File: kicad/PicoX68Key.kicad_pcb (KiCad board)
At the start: 2 copper layers, 33.9 x 69 mm, 21 parts, among them J1 LED_BOARD, J2 MD-70S, Q1 2N7000, Q2 2N7000, Q3 2N7000, U1 Pico

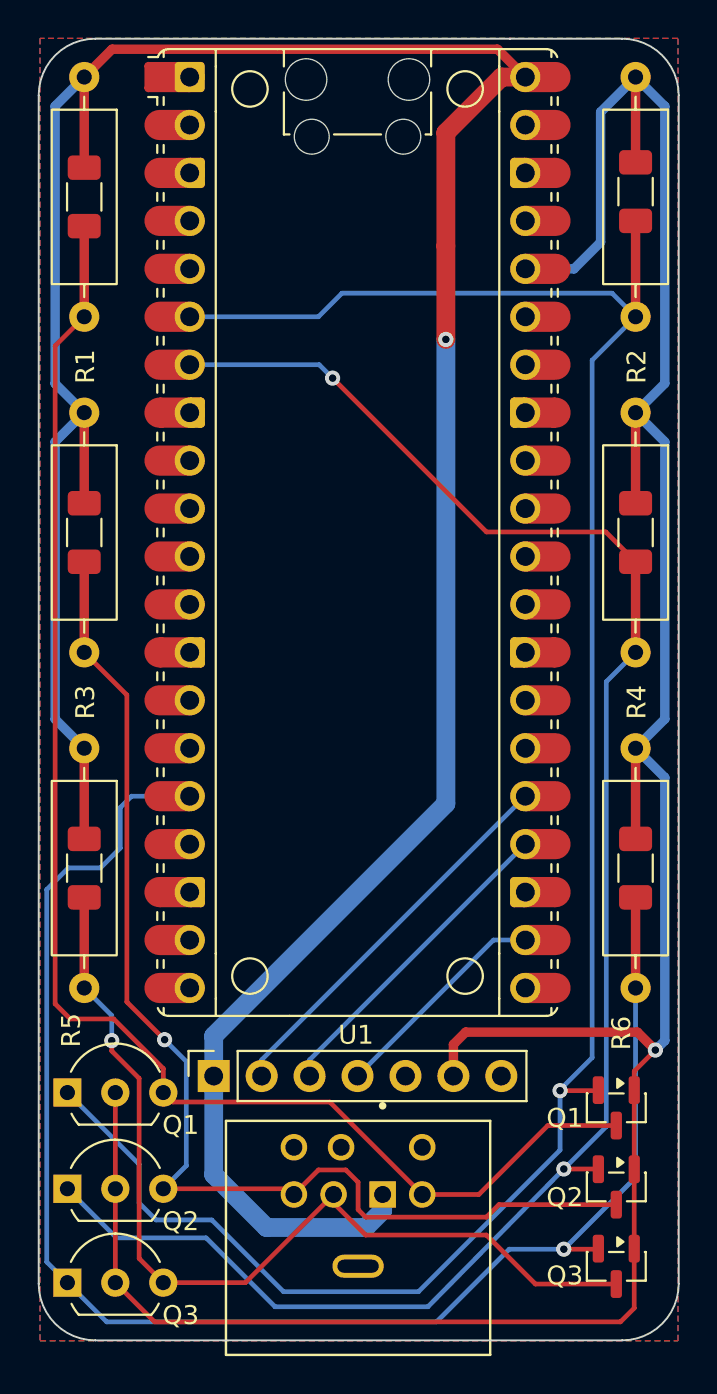
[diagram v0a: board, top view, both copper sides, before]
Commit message: Fix DIN footprint, board cleanup, silkscreen shenanigans
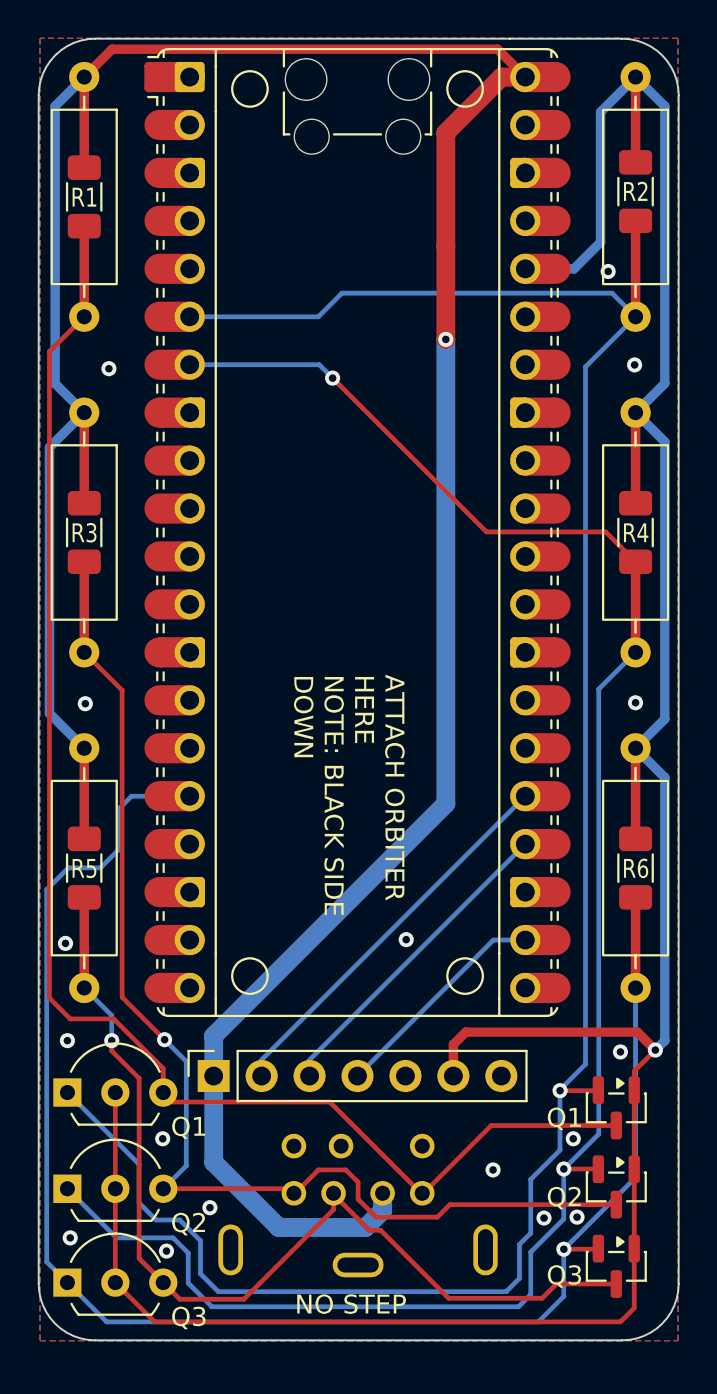
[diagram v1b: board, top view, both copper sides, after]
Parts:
- added G***: LOGO, Library:X68000_Logo, B.Cu at (83.8, 106.7)
- J1: footprint Library:PinSocket_1x07_P2.54mm_Vertical -> Connector_PinSocket_2.54mm:PinSocket_1x07_P2.54mm_Vertical
- J2: value MD-70S -> MINI-DIN-7; footprint Library:CUI_MD-70S -> Library:Mini_DIN_round_7_canned
- Q1, Q2, Q3: footprint Library:TO-92L_Inline_Wide -> Package_TO_SOT_THT:TO-92L_Inline_Wide
- R1, R2, R3, R4, R5, R6: footprint Library:R_Axial_DIN0309_L9.0mm_D3.2mm_P12.70mm_Horizontal -> Resistor_THT:R_Axial_DIN0309_L9.0mm_D3.2mm_P12.70mm_Horizontal
- R10, R11, R12, R7, R8, R9: footprint Library:R_1206_3216Metric_Pad1.30x1.75mm_HandSolder -> Resistor_SMD:R_1206_3216Metric_Pad1.30x1.75mm_HandSolder
- SQ1, SQ2, SQ3: footprint Library:SOT-23 -> Package_TO_SOT_SMD:SOT-23
- moved J2 4.64 mm to (83.8, 150.2), turned to 180 degrees
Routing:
- net KB_RX_L: track 95.7 -> 99.5 mm
- net KB_TX_L: track 112.6 -> 116.3 mm
- net MS_TX_H: track 50.3 -> 51.9 mm
- net MS_TX_L: track 83.5 -> 85.0 mm
- net GND: vias 0 -> 17
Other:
- board text added: "@retroswim@bitbang.social twitch.tv/retroswim"
- board text added: "ATTACH ORBITER HERE NOTE: BLACK SIDE DOWN"
- board text added: "Designed by RetroSwim"
- board text added: "Greets: ARB crew, polpo, FreddyV, fire PickledDog, CloakedAlien, Coburn64"
- board text added: "Key"
- board text added: "L_EN"
- board text added: "NO STEP"
- board text added: "Pico"
- board text added: "https://github.com/retroswimau/PicoX68Key"
- board text removed: "CS"
